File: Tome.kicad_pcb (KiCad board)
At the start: 2 copper layers, 153.1 x 139.6 mm, 147 parts, among them J1 USB_C_Receptacle_USB2.0_14P, J10 Conn_01x02_Pin, J11 Conn_01x02_Pin, J12 Conn_01x02_Pin, J13 Conn_01x02_Pin, J14 Conn_01x02_Pin, J15 Conn_01x02_Pin, J16 Conn_01x02_Pin, J17 Conn_01x02_Pin, J2 [battery], J3 SD_Card_Receptacle, J4 [bootstrap jumper], J5 AudioJack3, J6 FPC Connector, J7 FPC Connector, J8 FFC Connector, J9 FFC Connector, Q1 DMG3415, Q2 DMG3415, Q3 Si1308EDL, Q4 Si1308EDL, SW1 [reset button], SW2 SW_SPST, SW3 SW_SPST, SW4 RotaryEncoder_Switch, SW5 SW_SPST, SW6 RotaryEncoder_Switch, SW7 SW_SPST, U1 RP2040, U2 XC6220B331MR, U3 MCP73831-2-OT, U4 W25Q128JVS, U5 TLV70033_SOT23-5, U6 PCM5102A, U7 PAM8908, Y1 ABM8-272-T3

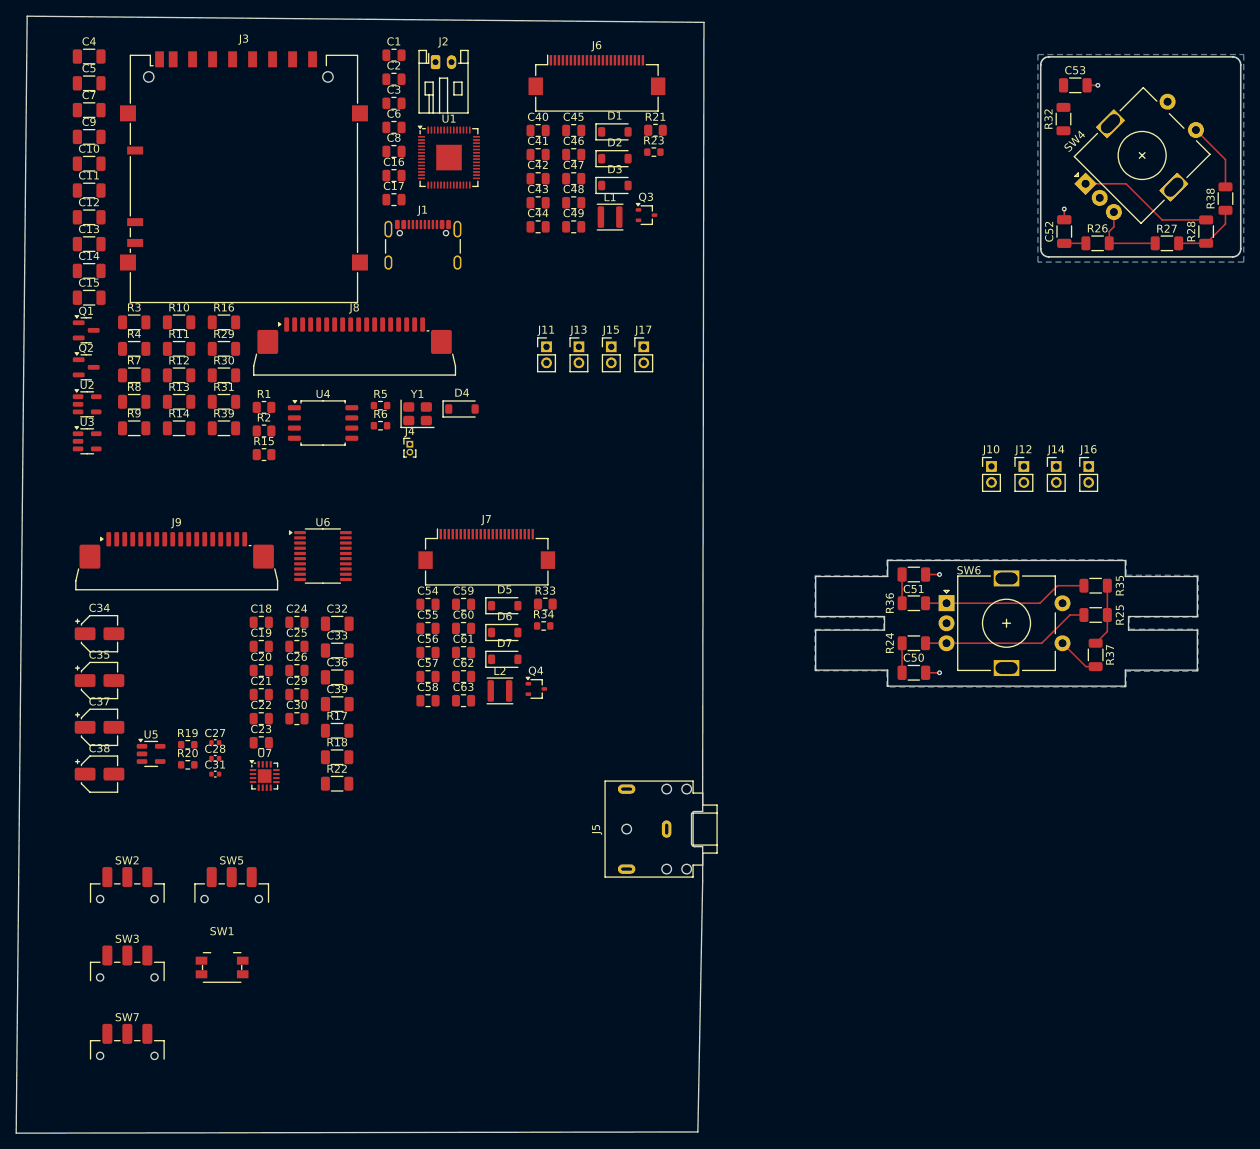
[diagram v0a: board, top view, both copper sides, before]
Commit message: update footprints and labeling
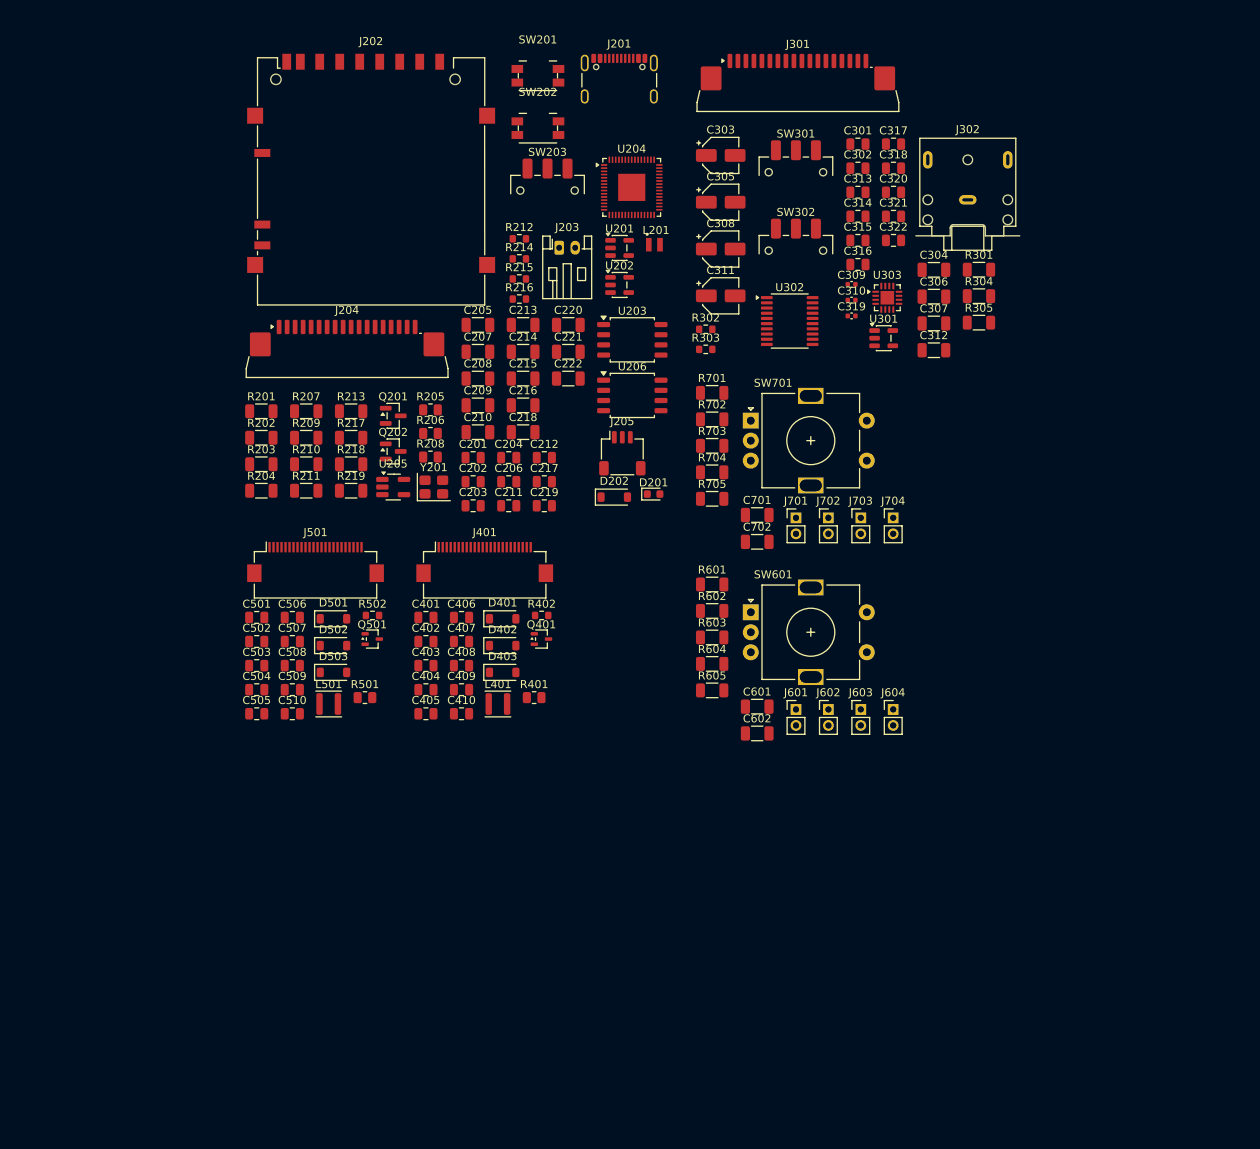
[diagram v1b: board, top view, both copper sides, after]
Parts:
- removed C1, C2, C3: 10u, Capacitor_SMD:C_0805_2012Metric
- removed C10, C11, C12, C13, C14, C15, C4, C5, C50, C51, C52, C53, C7, C9: 100n, Capacitor_SMD:C_1206_3216Metric
- removed C16, C17: 15p, Capacitor_SMD:C_0805_2012Metric
- removed C18, C19, C20, C21, C22, C23, C24, C25, C26, C6, C8: 1u, Capacitor_SMD:C_0805_2012Metric
- removed C27, C28, C31: 2.2u, Capacitor_SMD:C_0402_1005Metric
- removed C29, C30: 2.2n, Capacitor_SMD:C_0805_2012Metric
- removed C32, C33, C36, C39: 0.1u, Capacitor_SMD:C_1206_3216Metric
- removed C34, C35, C37, C38: 10u, Capacitor_SMD:CP_Elec_4x4.5
- removed C40, C41, C45, C54, C55, C59: 1uF, Capacitor_SMD:C_0805_2012Metric
- removed C42, C43, C44, C46, C47, C48, C49, C56, C57, C58, C60, C61, C62, C63: 4.7uF, Capacitor_SMD:C_0805_2012Metric
- removed D1, D2, D3, D5, D6, D7: MBR0530, Diode_SMD:D_SOD-123
- removed D4: MBR120, Diode_SMD:D_SOD-123
- removed J1: USB_C_Receptacle_USB2.0_14P, Connector_USB:USB_C_Receptacle_GCT_USB4105-xx-A_16P_TopMnt_Horizontal
- removed J10, J11, J12, J13, J14, J15, J16, J17: Conn_01x02_Pin, Connector_PinHeader_2.00mm:PinHeader_1x02_P2.00mm_Vertical
- removed J2: [battery], Connector_JST:JST_PH_S2B-PH-K_1x02_P2.00mm_Horizontal
- removed J3: SD_Card_Receptacle, Connector_Card:SD_Hirose_DM1AA_SF_PEJ82
- removed J4: [bootstrap jumper], Connector_PinHeader_1.00mm:PinHeader_1x02_P1.00mm_Vertical
- removed J5: AudioJack3, Connector_Audio:Jack_3.5mm_CUI_SJ1-3523N_Horizontal
- removed J6, J7: FPC Connector, Connector_FFC-FPC:Hirose_FH12-24S-0.5SH_1x24-1MP_P0.50mm_Horizontal
- removed J8, J9: FFC Connector, Connector_FFC-FPC:JUSHUO_AFA07-S18FCA-00_1x18-1MP_P1.0mm_Horizontal
- removed L1, L2: 47uH, Inductor_SMD:L_APV_ANR3015
- removed Q1, Q2: DMG3415, Package_TO_SOT_SMD:SOT-23
- removed Q3, Q4: Si1308EDL, Package_TO_SOT_SMD:SOT-323_SC-70
- removed R1, R2: 5.1k, Resistor_SMD:R_0805_2012Metric
- removed R10, R3, R9: 1k, Resistor_SMD:R_1206_3216Metric
- removed R11, R16, R17, R18, R22, R24, R25, R26, R27, R28, R29, R30, R31, R32, R35, R36, R37, R38, R39, R7, R8: 10k, Resistor_SMD:R_1206_3216Metric
- removed R12, R13, R14, R4: 100k, Resistor_SMD:R_1206_3216Metric
- removed R15: 200k, Resistor_SMD:R_0805_2012Metric
- removed R19, R20: 470, Resistor_SMD:R_0603_1608Metric
- removed R21, R33: 1M, Resistor_SMD:R_0805_2012Metric
- removed R23, R34: 2.2, Resistor_SMD:R_0603_1608Metric
- removed R5, R6: 27.4, Resistor_SMD:R_0603_1608Metric
- removed SW1: [reset button], Button_Switch_SMD:Panasonic_EVQPUK_EVQPUB
- removed SW2, SW3, SW5, SW7: SW_SPST, Button_Switch_SMD:SW_SPDT_CK_JS102011SAQN
- removed SW4, SW6: RotaryEncoder_Switch, Rotary_Encoder:RotaryEncoder_Alps_EC11E-Switch_Vertical_H20mm
- removed U1: RP2040, Package_DFN_QFN:QFN-56-1EP_7x7mm_P0.4mm_EP3.2x3.2mm
- removed U2: XC6220B331MR, Package_TO_SOT_SMD:SOT-23-5
- removed U3: MCP73831-2-OT, Package_TO_SOT_SMD:SOT-23-5
- removed U4: W25Q128JVS, Package_SO:SOIC-8_5.3x5.3mm_P1.27mm
- removed U5: TLV70033_SOT23-5, Package_TO_SOT_SMD:SOT-23-5
- removed U6: PCM5102A, Package_SO:TSSOP-20_4.4x6.5mm_P0.65mm
- removed U7: PAM8908, Package_DFN_QFN:QFN-16-1EP_3x3mm_P0.5mm_EP1.7x1.7mm
- removed Y1: ABM8-272-T3, Crystal:Crystal_SMD_3225-4Pin_3.2x2.5mm
- added C201: 10u, Capacitor_SMD:C_0805_2012Metric, F.Cu at (67.3, 65.7)
- added C202: 10u, Capacitor_SMD:C_0805_2012Metric, F.Cu at (67.3, 68.7)
- added C203: 10u, Capacitor_SMD:C_0805_2012Metric, F.Cu at (67.3, 71.7)
- added C204: 4.7u, Capacitor_SMD:C_0805_2012Metric, F.Cu at (71.8, 65.7)
- added C205: 100n, Capacitor_SMD:C_1206_3216Metric, F.Cu at (67.9, 49.1)
- added C206: 10u, Capacitor_SMD:C_0805_2012Metric, F.Cu at (71.8, 68.7)
- added C207: 100n, Capacitor_SMD:C_1206_3216Metric, F.Cu at (67.9, 52.4)
- added C208: 100n, Capacitor_SMD:C_1206_3216Metric, F.Cu at (67.9, 55.8)
- added C209: 100n, Capacitor_SMD:C_1206_3216Metric, F.Cu at (67.9, 59.1)
- added C210: 100n, Capacitor_SMD:C_1206_3216Metric, F.Cu at (67.9, 62.5)
- added C211: 15p, Capacitor_SMD:C_0805_2012Metric, F.Cu at (71.8, 71.7)
- added C212: 15p, Capacitor_SMD:C_0805_2012Metric, F.Cu at (76.2, 65.7)
- added C213: 100n, Capacitor_SMD:C_1206_3216Metric, F.Cu at (73.6, 49.1)
- added C214: 4.7u, Capacitor_SMD:C_1206_3216Metric, F.Cu at (73.6, 52.4)
- added C215: 100n, Capacitor_SMD:C_1206_3216Metric, F.Cu at (73.6, 55.8)
- added C216: 100n, Capacitor_SMD:C_1206_3216Metric, F.Cu at (73.6, 59.1)
- added C217: 4.7u, Capacitor_SMD:C_0805_2012Metric, F.Cu at (76.2, 68.7)
- added C218: 100n, Capacitor_SMD:C_1206_3216Metric, F.Cu at (73.6, 62.5)
- added C219: 4.7u, Capacitor_SMD:C_0805_2012Metric, F.Cu at (76.2, 71.7)
- added C220: 100n, Capacitor_SMD:C_1206_3216Metric, F.Cu at (79.2, 49.1)
- added C221: 100n, Capacitor_SMD:C_1206_3216Metric, F.Cu at (79.2, 52.4)
- added C222: 100n, Capacitor_SMD:C_1206_3216Metric, F.Cu at (79.2, 55.8)
- added C301: 1u, Capacitor_SMD:C_0805_2012Metric, F.Cu at (115.4, 26.5)
- added C302: 1u, Capacitor_SMD:C_0805_2012Metric, F.Cu at (115.4, 29.5)
- added C303: 10u, Capacitor_SMD:CP_Elec_4x4.5, F.Cu at (98.3, 27.9)
- added C304: 0.1u, Capacitor_SMD:C_1206_3216Metric, F.Cu at (124.9, 42.2)
- added C305: 10u, Capacitor_SMD:CP_Elec_4x4.5, F.Cu at (98.3, 33.7)
- added C306: 0.1u, Capacitor_SMD:C_1206_3216Metric, F.Cu at (124.9, 45.5)
- added C307: 0.1u, Capacitor_SMD:C_1206_3216Metric, F.Cu at (124.9, 48.9)
- added C308: 10u, Capacitor_SMD:CP_Elec_4x4.5, F.Cu at (98.3, 39.6)
- added C309: 2.2u, Capacitor_SMD:C_0402_1005Metric, F.Cu at (114.7, 44.0)
- added C310: 2.2u, Capacitor_SMD:C_0402_1005Metric, F.Cu at (114.7, 46.0)
- added C311: 10u, Capacitor_SMD:CP_Elec_4x4.5, F.Cu at (98.3, 45.4)
- added C312: 0.1u, Capacitor_SMD:C_1206_3216Metric, F.Cu at (124.9, 52.2)
- added C313: 2.2n, Capacitor_SMD:C_0805_2012Metric, F.Cu at (115.4, 32.5)
- added C314: 2.2n, Capacitor_SMD:C_0805_2012Metric, F.Cu at (115.4, 35.5)
- added C315: 1u, Capacitor_SMD:C_0805_2012Metric, F.Cu at (115.4, 38.5)
- added C316: 1u, Capacitor_SMD:C_0805_2012Metric, F.Cu at (115.4, 41.5)
- added C317: 1u, Capacitor_SMD:C_0805_2012Metric, F.Cu at (119.9, 26.5)
- added C318: 1u, Capacitor_SMD:C_0805_2012Metric, F.Cu at (119.9, 29.5)
- added C319: 2.2u, Capacitor_SMD:C_0402_1005Metric, F.Cu at (114.7, 47.9)
- added C320: 1u, Capacitor_SMD:C_0805_2012Metric, F.Cu at (119.9, 32.5)
- added C321: 1u, Capacitor_SMD:C_0805_2012Metric, F.Cu at (119.9, 35.5)
- added C322: 1u, Capacitor_SMD:C_0805_2012Metric, F.Cu at (119.9, 38.5)
- added C401: 1uF, Capacitor_SMD:C_0805_2012Metric, F.Cu at (61.4, 85.6)
- added C402: 1uF, Capacitor_SMD:C_0805_2012Metric, F.Cu at (61.4, 88.6)
- added C403: 4.7uF, Capacitor_SMD:C_0805_2012Metric, F.Cu at (61.4, 91.7)
- added C404: 4.7uF, Capacitor_SMD:C_0805_2012Metric, F.Cu at (61.4, 94.7)
- added C405: 4.7uF, Capacitor_SMD:C_0805_2012Metric, F.Cu at (61.4, 97.7)
- added C406: 1uF, Capacitor_SMD:C_0805_2012Metric, F.Cu at (65.9, 85.6)
- added C407: 4.7uF, Capacitor_SMD:C_0805_2012Metric, F.Cu at (65.9, 88.6)
- added C408: 4.7uF, Capacitor_SMD:C_0805_2012Metric, F.Cu at (65.9, 91.7)
- added C409: 4.7uF, Capacitor_SMD:C_0805_2012Metric, F.Cu at (65.9, 94.7)
- added C410: 4.7uF, Capacitor_SMD:C_0805_2012Metric, F.Cu at (65.9, 97.7)
- added C501: 1uF, Capacitor_SMD:C_0805_2012Metric, F.Cu at (40.3, 85.6)
- added C502: 1uF, Capacitor_SMD:C_0805_2012Metric, F.Cu at (40.3, 88.6)
- added C503: 4.7uF, Capacitor_SMD:C_0805_2012Metric, F.Cu at (40.3, 91.7)
- added C504: 4.7uF, Capacitor_SMD:C_0805_2012Metric, F.Cu at (40.3, 94.7)
- added C505: 4.7uF, Capacitor_SMD:C_0805_2012Metric, F.Cu at (40.3, 97.7)
- added C506: 1uF, Capacitor_SMD:C_0805_2012Metric, F.Cu at (44.7, 85.6)
- added C507: 4.7uF, Capacitor_SMD:C_0805_2012Metric, F.Cu at (44.7, 88.6)
- added C508: 4.7uF, Capacitor_SMD:C_0805_2012Metric, F.Cu at (44.7, 91.7)
- added C509: 4.7uF, Capacitor_SMD:C_0805_2012Metric, F.Cu at (44.7, 94.7)
- added C510: 4.7uF, Capacitor_SMD:C_0805_2012Metric, F.Cu at (44.7, 97.7)
- added C601: 100n, Capacitor_SMD:C_1206_3216Metric, F.Cu at (102.9, 96.8)
- added C602: 100n, Capacitor_SMD:C_1206_3216Metric, F.Cu at (102.9, 100.1)
- added C701: 100n, Capacitor_SMD:C_1206_3216Metric, F.Cu at (102.9, 72.8)
- added C702: 100n, Capacitor_SMD:C_1206_3216Metric, F.Cu at (102.9, 76.2)
- added D201: LED, LED_SMD:LED_0603_1608Metric, F.Cu at (89.9, 70.2)
- added D202: MBR120, Diode_SMD:D_SOD-123, F.Cu at (85.0, 70.6)
- added D401: MBR0530, Diode_SMD:D_SOD-123, F.Cu at (71.0, 85.8)
- added D402: MBR0530, Diode_SMD:D_SOD-123, F.Cu at (71.0, 89.2)
- added D403: MBR0530, Diode_SMD:D_SOD-123, F.Cu at (71.0, 92.5)
- added D501: MBR0530, Diode_SMD:D_SOD-123, F.Cu at (49.9, 85.8)
- added D502: MBR0530, Diode_SMD:D_SOD-123, F.Cu at (49.9, 89.2)
- added D503: MBR0530, Diode_SMD:D_SOD-123, F.Cu at (49.9, 92.5)
- added J201: USB_C_Receptacle_USB2.0_14P, Connector_USB:USB_C_Receptacle_GCT_USB4105-xx-A_16P_TopMnt_Horizontal, F.Cu at (85.6, 19.4)
- added J202: SD_Card_Receptacle, Connector_Card:SD_Hirose_DM1AA_SF_PEJ82, F.Cu at (54.6, 31.1)
- added J203: [battery], Connector_JST:JST_PH_S2B-PH-K_1x02_P2.00mm_Horizontal, F.Cu at (78.1, 39.4)
- added J204: FFC Connector, Connector_FFC-FPC:JUSHUO_AFA07-S18FCA-00_1x18-1MP_P1.0mm_Horizontal, F.Cu at (51.6, 52.7)
- added J205: SM03B-SRSS-TB, Connector_JST:JST_SH_SM03B-SRSS-TB_1x03-1MP_P1.00mm_Horizontal, F.Cu at (86.0, 65.1)
- added J301: FFC Connector, Connector_FFC-FPC:JUSHUO_AFA07-S18FCA-00_1x18-1MP_P1.0mm_Horizontal, F.Cu at (107.9, 19.5)
- added J302: AudioJack3, Connector_Audio:Jack_3.5mm_CUI_SJ1-3523N_Horizontal, F.Cu at (129.2, 33.4)
- added J401: FPC Connector, Connector_FFC-FPC:Hirose_FH12-24S-0.5SH_1x24-1MP_P0.50mm_Horizontal, F.Cu at (68.8, 78.7)
- added J501: FPC Connector, Connector_FFC-FPC:Hirose_FH12-24S-0.5SH_1x24-1MP_P0.50mm_Horizontal, F.Cu at (47.6, 78.7)
- added J601: Conn_01x02_Pin, Connector_PinHeader_2.00mm:PinHeader_1x02_P2.00mm_Vertical, F.Cu at (107.7, 97.1)
- added J602: Conn_01x02_Pin, Connector_PinHeader_2.00mm:PinHeader_1x02_P2.00mm_Vertical, F.Cu at (111.8, 97.1)
- added J603: Conn_01x02_Pin, Connector_PinHeader_2.00mm:PinHeader_1x02_P2.00mm_Vertical, F.Cu at (115.8, 97.1)
- added J604: Conn_01x02_Pin, Connector_PinHeader_2.00mm:PinHeader_1x02_P2.00mm_Vertical, F.Cu at (119.9, 97.1)
- added J701: Conn_01x02_Pin, Connector_PinHeader_2.00mm:PinHeader_1x02_P2.00mm_Vertical, F.Cu at (107.7, 73.2)
- added J702: Conn_01x02_Pin, Connector_PinHeader_2.00mm:PinHeader_1x02_P2.00mm_Vertical, F.Cu at (111.8, 73.2)
- added J703: Conn_01x02_Pin, Connector_PinHeader_2.00mm:PinHeader_1x02_P2.00mm_Vertical, F.Cu at (115.8, 73.2)
- added J704: Conn_01x02_Pin, Connector_PinHeader_2.00mm:PinHeader_1x02_P2.00mm_Vertical, F.Cu at (119.9, 73.2)
- added L201: 3.3u, RP2350_80QFN_minimal:L_pol_2016, F.Cu at (90.0, 39.0)
- added L401: 47uH, Inductor_SMD:L_APV_ANR3015, F.Cu at (70.4, 96.5)
- added L501: 47uH, Inductor_SMD:L_APV_ANR3015, F.Cu at (49.3, 96.5)
- added Q201: DMG3415, Package_TO_SOT_SMD:SOT-23, F.Cu at (57.4, 60.4)
- added Q202: DMG3415, Package_TO_SOT_SMD:SOT-23, F.Cu at (57.4, 64.9)
- added Q401: Si1308EDL, Package_TO_SOT_SMD:SOT-323_SC-70, F.Cu at (75.9, 88.3)
- added Q501: Si1308EDL, Package_TO_SOT_SMD:SOT-323_SC-70, F.Cu at (54.7, 88.3)
- added R201: 1k, Resistor_SMD:R_1206_3216Metric, F.Cu at (40.9, 59.9)
- added R202: 87, Resistor_SMD:R_1206_3216Metric, F.Cu at (40.9, 63.2)
- added R203: 100k, Resistor_SMD:R_1206_3216Metric, F.Cu at (40.9, 66.5)
- added R204: 100k, Resistor_SMD:R_1206_3216Metric, F.Cu at (40.9, 69.8)
- added R205: 5.1k, Resistor_SMD:R_0805_2012Metric, F.Cu at (62.0, 59.7)
- added R206: 5.1k, Resistor_SMD:R_0805_2012Metric, F.Cu at (62.0, 62.6)
- added R207: 100k, Resistor_SMD:R_1206_3216Metric, F.Cu at (46.5, 59.9)
- added R208: 200k, Resistor_SMD:R_0805_2012Metric, F.Cu at (62.0, 65.6)
- added R209: 100k, Resistor_SMD:R_1206_3216Metric, F.Cu at (46.5, 63.2)
- added R210: 1k, Resistor_SMD:R_1206_3216Metric, F.Cu at (46.5, 66.5)
- added R211: 10k, Resistor_SMD:R_1206_3216Metric, F.Cu at (46.5, 69.8)
- added R212: 1k, Resistor_SMD:R_0603_1608Metric, F.Cu at (73.1, 38.3)
- added R213: 1k, Resistor_SMD:R_1206_3216Metric, F.Cu at (52.1, 59.9)
- added R214: 27.4, Resistor_SMD:R_0603_1608Metric, F.Cu at (73.1, 40.8)
- added R215: 27.4, Resistor_SMD:R_0603_1608Metric, F.Cu at (73.1, 43.3)
- added R216: 33, Resistor_SMD:R_0603_1608Metric, F.Cu at (73.1, 45.8)
- added R217: 10k, Resistor_SMD:R_1206_3216Metric, F.Cu at (52.1, 63.2)
- added R218: 10k, Resistor_SMD:R_1206_3216Metric, F.Cu at (52.1, 66.5)
- added R219: 10k, Resistor_SMD:R_1206_3216Metric, F.Cu at (52.1, 69.8)
- added R301: 10k, Resistor_SMD:R_1206_3216Metric, F.Cu at (130.6, 42.2)
- added R302: 470, Resistor_SMD:R_0603_1608Metric, F.Cu at (96.4, 49.6)
- added R303: 470, Resistor_SMD:R_0603_1608Metric, F.Cu at (96.4, 52.1)
- added R304: 10k, Resistor_SMD:R_1206_3216Metric, F.Cu at (130.6, 45.5)
- added R305: 10k, Resistor_SMD:R_1206_3216Metric, F.Cu at (130.6, 48.8)
- added R401: 1M, Resistor_SMD:R_0805_2012Metric, F.Cu at (75.0, 95.7)
- added R402: 2.2, Resistor_SMD:R_0603_1608Metric, F.Cu at (75.9, 85.4)
- added R501: 1M, Resistor_SMD:R_0805_2012Metric, F.Cu at (53.8, 95.7)
- added R502: 2.2, Resistor_SMD:R_0603_1608Metric, F.Cu at (54.8, 85.4)
- added R601: 10k, Resistor_SMD:R_1206_3216Metric, F.Cu at (97.2, 81.5)
- added R602: 10k, Resistor_SMD:R_1206_3216Metric, F.Cu at (97.2, 84.8)
- added R603: 10k, Resistor_SMD:R_1206_3216Metric, F.Cu at (97.2, 88.1)
- added R604: 10k, Resistor_SMD:R_1206_3216Metric, F.Cu at (97.2, 91.4)
- added R605: 10k, Resistor_SMD:R_1206_3216Metric, F.Cu at (97.2, 94.8)
- added R701: 10k, Resistor_SMD:R_1206_3216Metric, F.Cu at (97.2, 57.6)
- added R702: 10k, Resistor_SMD:R_1206_3216Metric, F.Cu at (97.2, 60.9)
- added R703: 10k, Resistor_SMD:R_1206_3216Metric, F.Cu at (97.2, 64.2)
- added R704: 10k, Resistor_SMD:R_1206_3216Metric, F.Cu at (97.2, 67.5)
- added R705: 10k, Resistor_SMD:R_1206_3216Metric, F.Cu at (97.2, 70.8)
- added SW201: [bootstrap button], Button_Switch_SMD:Panasonic_EVQPUK_EVQPUB, F.Cu at (75.4, 17.9)
- added SW202: [reset button], Button_Switch_SMD:Panasonic_EVQPUK_EVQPUB, F.Cu at (75.4, 24.5)
- added SW203: SW_SPST, Button_Switch_SMD:SW_SPDT_CK_JS102011SAQN, F.Cu at (76.6, 32.3)
- added SW301: SW_SPST, Button_Switch_SMD:SW_SPDT_CK_JS102011SAQN, F.Cu at (107.7, 30.0)
- added SW302: SW_SPST, Button_Switch_SMD:SW_SPDT_CK_JS102011SAQN, F.Cu at (107.7, 39.8)
- added SW601: RotaryEncoder_Switch, Rotary_Encoder:RotaryEncoder_Alps_EC11E-Switch_Vertical_H20mm, F.Cu at (102.1, 85.0)
- added SW701: RotaryEncoder_Switch, Rotary_Encoder:RotaryEncoder_Alps_EC11E-Switch_Vertical_H20mm, F.Cu at (102.1, 61.0)
- added U201: MCP73831-2-OT, Package_TO_SOT_SMD:SOT-23-5, F.Cu at (85.7, 39.5)
- added U202: XC6220B331MR, Package_TO_SOT_SMD:SOT-23-5, F.Cu at (85.7, 44.1)
- added U203: W25Q128JVS, Package_SO:SOIC-8_5.3x5.3mm_P1.27mm, F.Cu at (87.2, 50.9)
- added U204: RP2350A, Package_DFN_QFN:QFN-60-1EP_7x7mm_P0.4mm_EP3.4x3.4mm, F.Cu at (87.2, 31.9)
- added U205: 74AHC1G04, Package_TO_SOT_SMD:SOT-23-5_HandSoldering, F.Cu at (57.4, 69.3)
- added U206: W25Q128JVS, Package_SO:SOIC-8_5.3x5.3mm_P1.27mm, F.Cu at (87.2, 57.9)
- added U301: TLV70033_SOT23-5, Package_TO_SOT_SMD:SOT-23-5, F.Cu at (118.7, 50.7)
- added U302: PCM5102A, Package_SO:TSSOP-20_4.4x6.5mm_P0.65mm, F.Cu at (106.9, 48.6)
- added U303: PAM8908, Package_DFN_QFN:QFN-16-1EP_3x3mm_P0.5mm_EP1.7x1.7mm, F.Cu at (119.1, 45.7)
- added Y201: ABM8-272-T3, Crystal:Crystal_SMD_3225-4Pin_3.2x2.5mm, F.Cu at (62.4, 69.3)
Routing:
- net Net-(R24-Pad2): track 21.3 -> 0.00 mm
- net Net-(R35-Pad2): track 20.7 -> 0.00 mm
- net Net-(R28-Pad2): track 16.9 -> 0.00 mm
- net +3.3VP: track 16.4 -> 0.00 mm
- net Net-(R26-Pad2): track 9.89 -> 0.00 mm
- net ENCODER_2_PUSH: track 8.64 -> 0.00 mm
- net GND: track 6.16 -> 0.00 mm, vias 4 -> 0
- net ENCODER_1_PUSH: track 5.35 -> 0.00 mm
- net ENCODER_1_B: track 3.70 -> 0.00 mm
- net ENCODER_1_A: track 3.60 -> 0.00 mm
- net ENCODER_2_B: track 2.70 -> 0.00 mm
- removed copper zone on B.Cu, net GND
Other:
- board size 153.1 x 139.6 mm -> 13 x 1.4 mm

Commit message: grouping
grouping components together based on schematic to organize things, in prep for arranging them for routing
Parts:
- moved R219 228.4 mm to (280.1, 54.8)
- moved J204 227.6 mm to (264.5, 133.0)
- moved Q202 226.8 mm to (265.3, 155.6)
- moved C206 212.0 mm to (275.9, 126.0)
- moved R217 194.5 mm to (246.4, 72.7)
- moved R207 194.4 mm to (222.4, 142.4), turned to -90 degrees
- moved R218 192.2 mm to (243.0, 88.4)
- moved U205 191.7 mm to (245.0, 108.7)
- moved R204 191.3 mm to (215.6, 147.6), turned to 90 degrees
- moved R203 190.3 mm to (215.5, 142.2), turned to 90 degrees
- moved C221 186.6 mm to (265.8, 55.0)
- moved U206 186.6 mm to (273.8, 60.5)
- moved SW203 185.7 mm to (253.0, 90.5)
- moved C501 184.0 mm to (64.0, -96.8)
- moved C502 184.0 mm to (64.0, -93.8)
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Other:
- board text added: "ANALOG POWER"
- board text added: "AUDIO OUT (DAC + AMP + JACK)"
- board text added: "BATTERY + MONITORING"
- board text added: "ENCODER DAUGHTERBOARD"
- board text added: "ENCODER DAUGHTERBOARD PERI"
- board text added: "INTERCONNECT"
- board text added: "INTERCONNECT PERI"
- board text added: "PERIPHERAL POWER CONTROL"
- board text added: "RP2350(A) + FLASH + CRYSTAL"
- board text added: "SCREEN DAUGHTERBOARD"
- board text added: "SCREEN DAUGHTERBOARD PERI"
- board text added: "SD CARD SLOT"
- board text added: "USB + POWER"

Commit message: Update Tome.kicad_pcb
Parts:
- moved C406 234.9 mm to (49.7, 137.9)
- moved D402 231.6 mm to (93.9, 133.9)
- moved J401 230.6 mm to (56.5, 126.6), turned to 90 degrees
- moved C408 228.9 mm to (87.0, 134.0)
- moved D401 228.4 mm to (87.2, 128.6)
- moved R402 227.2 mm to (79.6, 128.6)
- moved C410 227.2 mm to (102.6, 134.7)
- moved D403 226.5 mm to (100.2, 130.7)
- moved C403 226.1 mm to (45.4, 135.1)
- moved C402 222.4 mm to (45.4, 128.4)
- moved C409 221.9 mm to (93.8, 128.5)
- moved C401 220.7 mm to (45.5, 123.7)
- moved Q401 217.7 mm to (79.5, 122.0)
- moved C405 216.5 mm to (49.8, 131.4)
- moved R401 216.4 mm to (74.9, 128.4)
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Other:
- board text added: "BOOST CONVERTER"
- board text added: "SCREEN CONNECTOR"

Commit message: voltage regulator circuit
routed the voltage regulator circuit following strongly suggested layout from the rp2350 hardware design doc, sized decoupling capacitors down
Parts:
- C204, C217, C219, C403, C404, C405, C407, C408, C409, C410, C503, C504, C505, C507, C508, C509, C510: footprint Capacitor_SMD:C_0805_2012Metric -> Capacitor_SMD:C_0402_1005Metric
- C205, C207, C208, C209, C210, C213, C214, C215, C216, C218, C220, C221, C222, C601, C602, C701, C702: footprint Capacitor_SMD:C_1206_3216Metric -> Capacitor_SMD:C_0402_1005Metric
- moved C204 52.9 mm to (263.0, 35.5)
- moved U204 43.7 mm to (261.0, 40.5)
- moved C217 27.7 mm to (263.0, 34.4)
- moved C205 24.5 mm to (189.0, 49.7)
- moved C216 23.3 mm to (232.3, 60.8)
- moved C220 18.5 mm to (249.6, 54.7)
- moved C208 16.5 mm to (194.2, 49.7)
- moved C213 15.2 mm to (209.8, 50.0)
- moved C209 10.4 mm to (199.5, 49.9)
- moved C215 7.75 mm to (215.2, 50.0)
- moved L201 7.19 mm to (263.0, 32.4)
- moved C218 6.54 mm to (238.8, 54.7)
- moved C219 4.50 mm to (244.2, 54.5)
- moved C210 4.44 mm to (204.7, 50.0)
- moved SW201 3.38 mm to (180.7, 63.2)
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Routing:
- net +3V3: track 0.00 -> 7.51 mm
- net +1V1: track 0.00 -> 6.38 mm, vias 0 -> 3
- net GND: vias 0 -> 2
- added copper zone on F.Cu, net +1V1
- added copper zone on F.Cu, net +3V3
- added copper zone on F.Cu, net GND
- added copper zone on F.Cu, net Net-(U204-VREG_LX)

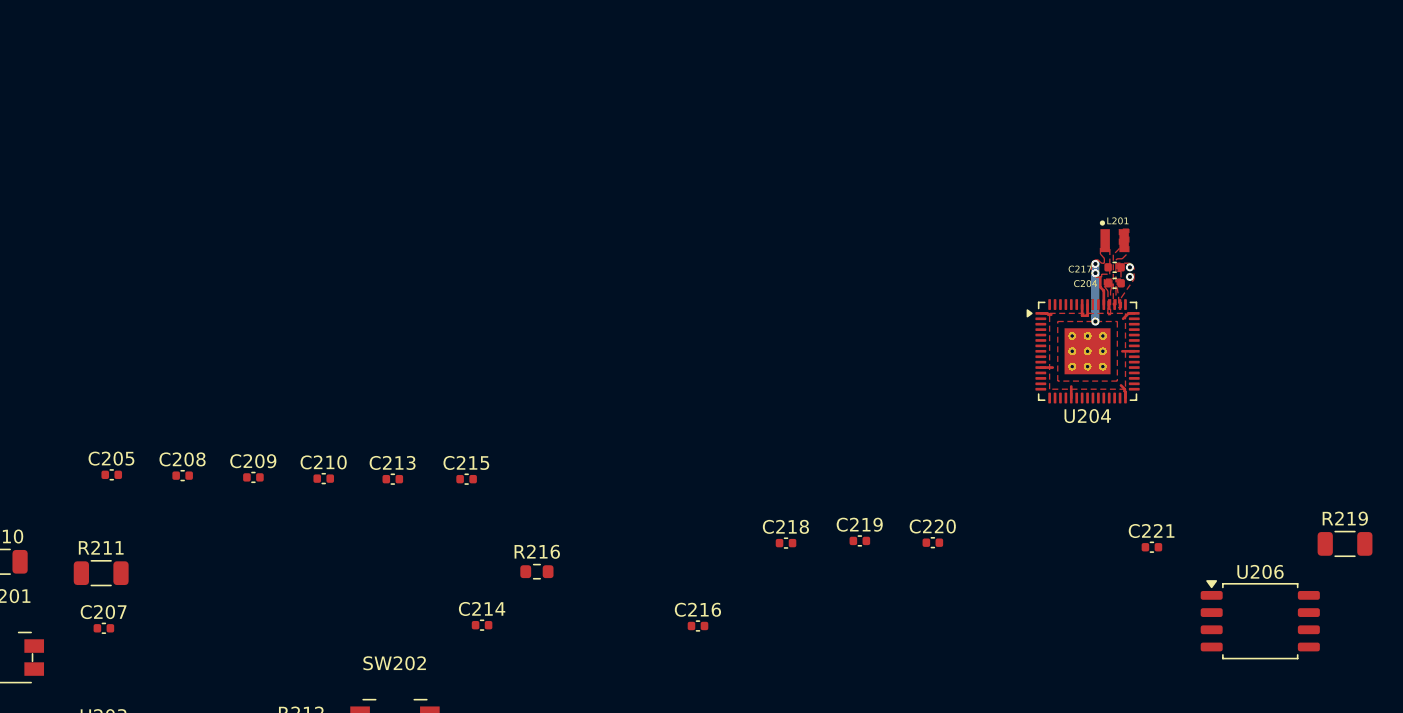
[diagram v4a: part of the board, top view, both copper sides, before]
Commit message: started placing decoupling capacitors
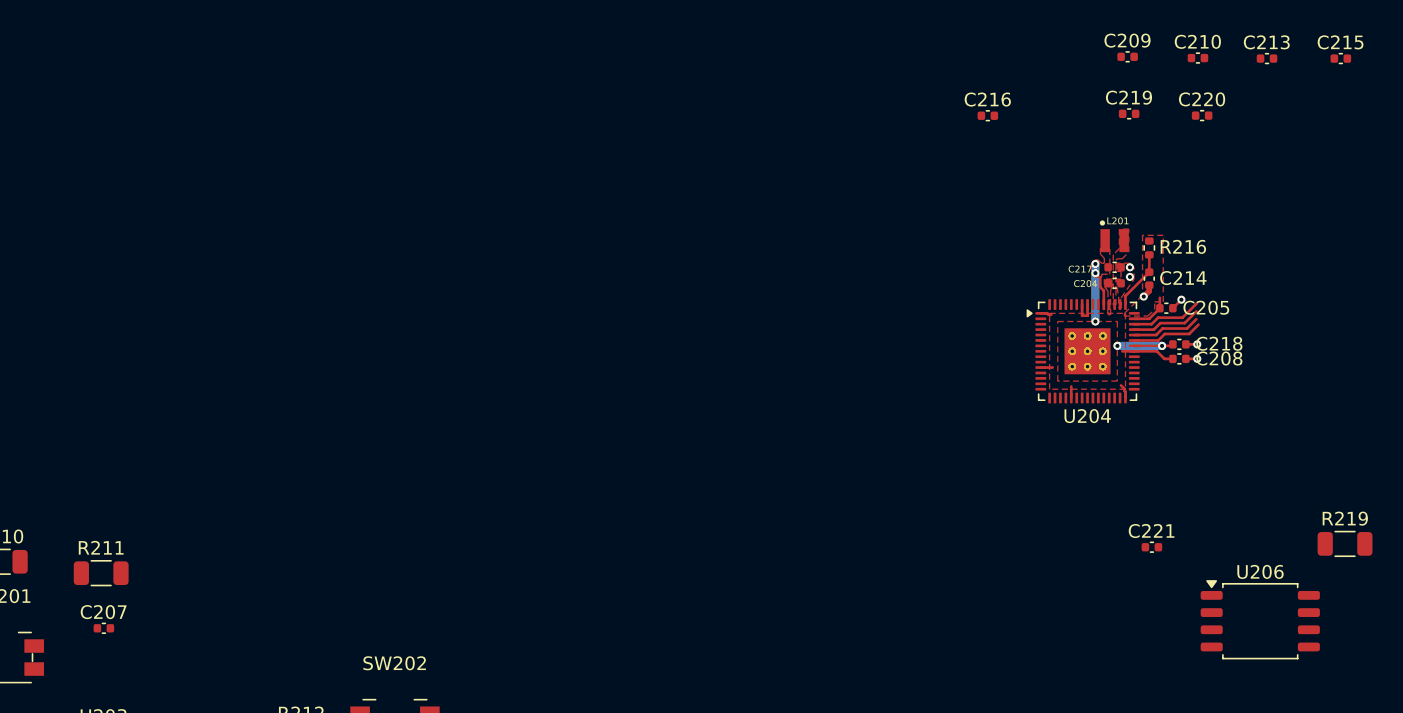
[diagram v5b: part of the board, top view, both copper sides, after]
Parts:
- R216: footprint Resistor_SMD:R_0603_1608Metric -> Resistor_SMD:R_0402_1005Metric
- moved C205 78.8 mm to (266.9, 37.4)
- moved C208 74.1 mm to (267.8, 41.1)
- moved C213 71.6 mm to (274.3, 18.9)
- moved C215 71.6 mm to (279.7, 18.9)
- moved C209 71.6 mm to (264.0, 18.8)
- moved C210 71.6 mm to (269.2, 18.9)
- moved C214 55.5 mm to (265.6, 35.2), turned to -90 degrees
- moved R216 51.1 mm to (265.6, 32.9), turned to 90 degrees
- moved C216 43.3 mm to (253.7, 23.2)
- moved C219 37.3 mm to (264.1, 23.0)
- moved C220 37.3 mm to (269.5, 23.1)
- moved C218 32.5 mm to (267.8, 40.0)
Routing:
- net +1V1: track 6.38 -> 12.6 mm, vias 3 -> 5
- net BUS_MONITOR: track 0.00 -> 5.26 mm
- net ENCODER_2_PUSH: track 0.00 -> 5.23 mm
- net BATT_MONITOR: track 0.00 -> 5.14 mm
- net +3V3: track 7.51 -> 12.6 mm
- net PERIPHERAL_ENABLE: track 0.00 -> 5.07 mm
- net Net-(U204-VREG_AVDD): track 0.00 -> 4.40 mm
- net GND: track 0.00 -> 3.58 mm, vias 2 -> 6

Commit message: crystal oscillator
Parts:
- C211, C212: footprint Capacitor_SMD:C_0805_2012Metric -> Capacitor_SMD:C_0402_1005Metric
- R213: footprint Resistor_SMD:R_1206_3216Metric -> Resistor_SMD:R_0402_1005Metric
- moved C203 111.5 mm to (233.4, 46.5)
- moved Q201 111.5 mm to (228.2, 34.8)
- moved R206 111.5 mm to (222.0, 40.4)
- moved U202 111.5 mm to (235.1, 37.6)
- moved D202 111.5 mm to (228.7, 41.2)
- moved J201 111.5 mm to (212.8, 39.4)
- moved R205 111.5 mm to (222.0, 37.4)
- moved R209 111.5 mm to (224.5, 46.3)
- moved C212 78.7 mm to (262.6, 50.2)
- moved C211 73.3 mm to (259.6, 50.2), turned to 180 degrees
- moved R213 72.3 mm to (260.8, 47.6), turned to -90 degrees
- moved Y201 68.9 mm to (261.0, 53.1)
- moved C215 31.6 mm to (254.2, 37.6)
- moved C213 30.4 mm to (254.8, 42.3)
- moved C210 29.8 mm to (259.1, 47.0), turned to -90 degrees
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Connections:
- R213 pad 1: Net-(C212-Pad1) -> Net-(U204-XOUT)
- R213 pad 2: Net-(U204-XOUT) -> Net-(C212-Pad1)
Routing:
- net Net-(U204-XIN): track 0.00 -> 10.9 mm
- net +1V1: track 12.6 -> 19.5 mm, vias 5 -> 7
- net Net-(J205-Pin_1): track 0.00 -> 5.14 mm
- net +3V3: track 12.6 -> 17.6 mm
- net GND: track 3.58 -> 8.59 mm, vias 6 -> 13
- net Net-(C212-Pad1): track 0.00 -> 4.74 mm
- net DISPLAY_RESET_L: track 0.00 -> 4.71 mm
- net Net-(J205-Pin_3): track 0.00 -> 4.66 mm
- net ENCODER_2_B: track 0.00 -> 4.40 mm
- net ENCODER_2_A: track 0.00 -> 4.23 mm
- net DISPLAY_DC: track 0.00 -> 4.21 mm
- net Net-(U204-RUN): track 0.00 -> 4.16 mm
- net ENCODER_1_PUSH: track 0.00 -> 4.07 mm
- net ENCODER_1_B: track 0.00 -> 3.90 mm
- net ENCODER_1_A: track 0.00 -> 3.74 mm
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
